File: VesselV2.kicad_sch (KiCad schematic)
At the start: 219 parts, among them SW1 SW_Push, U1 ATmega32U4-A, Y1 16MHz

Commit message: Switch footprint swap - 3d models fixed - Routing (re)done - No errors other than USB footprint
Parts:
- MX1, MX10, MX100, MX101, MX102, MX11, MX12, MX13, MX14, MX15, MX16, MX17, MX18, MX19, MX2, MX20, MX21, MX22, MX23, MX24, MX25, MX26, MX27, MX28, MX29, MX3, MX30, MX31, MX32, MX33, MX34, MX35, MX36, MX37, MX38, MX39, MX4, MX40, MX41, MX42, MX43, MX44, MX46, MX47, MX49, MX5, MX50, MX51, MX52, MX53, MX54, MX55, MX56, MX57, MX58, MX59, MX6, MX60, MX62, MX63, MX65, MX66, MX67, MX68, MX69, MX7, MX70, MX71, MX72, MX73, MX74, MX75, MX76, MX77, MX78, MX8, MX80, MX81, MX82, MX83, MX84, MX85, MX86, MX87, MX88, MX89, MX9, MX90, MX92, MX93: footprint PCM_marbastlib-mx:SW_MX_1u -> PCM_Switch_Keyboard_Cherry_MX:SW_Cherry_MX_PCB_1.00u
- MX45: footprint PCM_marbastlib-mx:SW_MX_1u -> PCM_Switch_Keyboard_Cherry_MX:SW_Cherry_MX_PCB_2.00u
- MX48: footprint PCM_marbastlib-mx:SW_MX_1.5u -> PCM_Switch_Keyboard_Cherry_MX:SW_Cherry_MX_PCB_1.50u
- MX61: footprint PCM_marbastlib-mx:SW_MX_1u -> PCM_Switch_Keyboard_Cherry_MX:SW_Cherry_MX_PCB_ISOEnter
- MX64, MX91: footprint PCM_marbastlib-mx:SW_MX_1.75u -> PCM_Switch_Keyboard_Cherry_MX:SW_Cherry_MX_PCB_1.75u
- MX79, MX94, MX95, MX96, MX98, MX99: footprint PCM_marbastlib-mx:SW_MX_1.25u -> PCM_Switch_Keyboard_Cherry_MX:SW_Cherry_MX_PCB_1.25u
- MX97: footprint PCM_marbastlib-mx:SW_MX_1u -> PCM_Switch_Keyboard_Cherry_MX:SW_Cherry_MX_PCB_6.25u
- S1: footprint PCM_marbastlib-mx:STAB_MX_P_2u -> PCM_Mounting_Keyboard_Stabilizer:Stabilizer_Cherry_MX_2.00u
- S2: footprint PCM_marbastlib-mx:STAB_MX_P_ISO -> PCM_Mounting_Keyboard_Stabilizer:Stabilizer_Cherry_MX_2.00u
- S3: footprint PCM_marbastlib-mx:STAB_MX_P_6.25u -> PCM_Mounting_Keyboard_Stabilizer:Stabilizer_Cherry_MX_6.25u

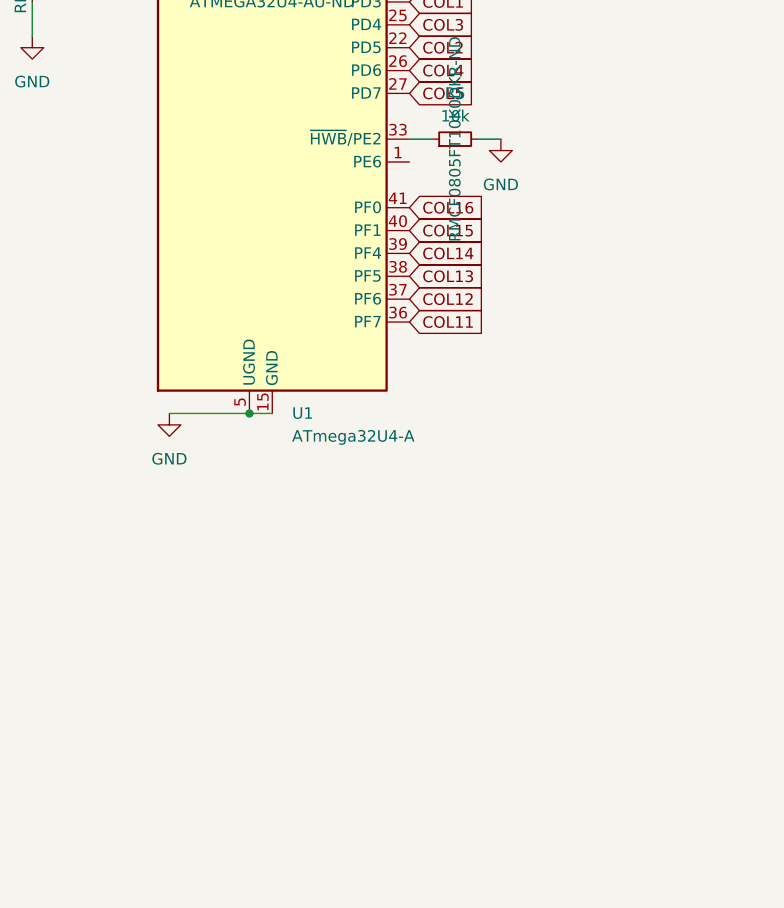
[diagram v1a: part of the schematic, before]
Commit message: Led Logo symbol and added - useless files deleted
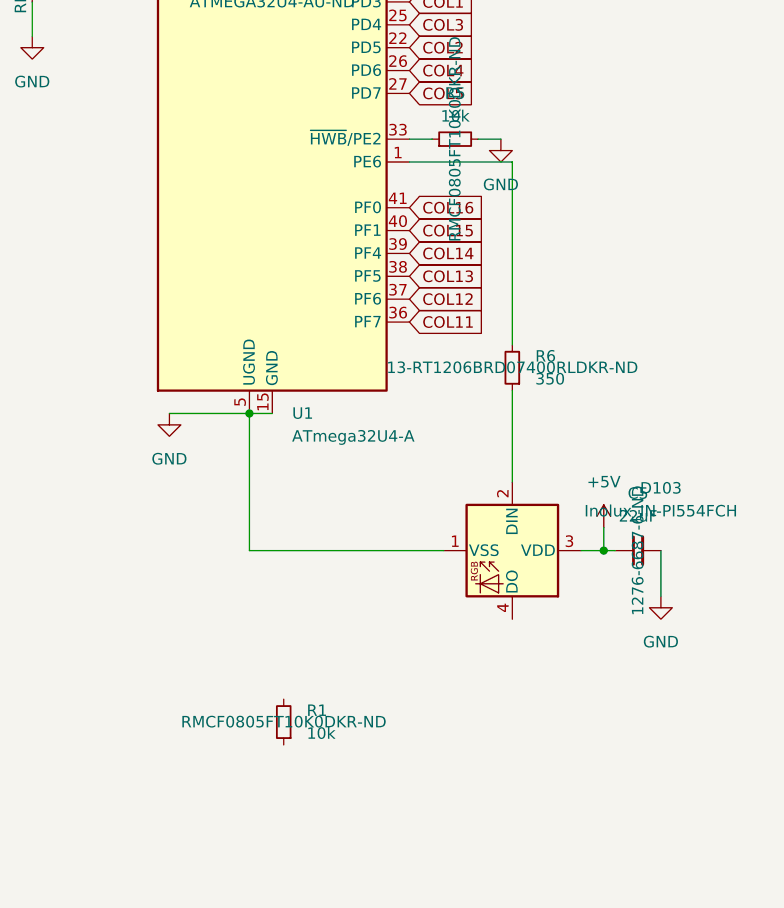
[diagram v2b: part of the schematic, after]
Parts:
- added C5: 22uF, Capacitor_SMD:C_0805_2012Metric_Pad1.18x1.45mm_HandSolder, symbol Device:C_Small
- added D103: Inolux_IN-PI554FCH, LED_SMD:LED_Inolux_IN-PI554FCH_PLCC4_5.0x5.0mm_P3.2mm, symbol LED:Inolux_IN-PI554FCH
- added R1: 10k, Resistor_SMD:R_0805_2012Metric_Pad1.20x1.40mm_HandSolder, symbol Device:R_Small
- added R6: 350, Resistor_SMD:R_0805_2012Metric_Pad1.20x1.40mm_HandSolder, symbol Device:R_Small
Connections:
- net +5V: now also C5.1, D103.3 (VDD)
- net GND: now also C5.2, D103.1 (VSS)
- net at U1.1 (PE6): now also R6.2
- new net: D103.2 (DIN), R6.1
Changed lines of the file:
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@@
   (junction (at 102.87 153.67) (diameter 0) (color 0 0 0 0)
   )
+  (junction (at 398.78 167.64) (diameter 0) (color 0 0 0 0)
+  )
   (junction (at 210.82 147.32) (diameter 0) (color 0 0 0 0)
   )
@@
     (stroke (width 0) (type default))
   )
+  (wire (pts (xy 388.62 149.86) (xy 388.62 160.02))
+    (stroke (width 0) (type default))
+  )
   (wire (pts (xy 176.53 198.12) (xy 187.96 198.12))
     (stroke (width 0) (type default))
@@
     (stroke (width 0) (type default))
   )
+  (wire (pts (xy 398.78 165.1) (xy 398.78 167.64))
+    (stroke (width 0) (type default))
+  )
   (wire (pts (xy 199.39 198.12) (xy 210.82 198.12))
     (stroke (width 0) (type default))
@@
     (stroke (width 0) (type default))
   )
+  (wire (pts (xy 405.13 167.64) (xy 405.13 172.72))
+    (stroke (width 0) (type default))
+  )
   (wire (pts (xy 210.82 147.32) (xy 222.25 147.32))
     (stroke (width 0) (type default))
@@
     (stroke (width 0) (type default))
   )
+  (wire (pts (xy 388.62 124.46) (xy 388.62 144.78))
+    (stroke (width 0) (type default))
+  )
   (wire (pts (xy 80.01 97.79) (xy 80.01 116.84))
     (stroke (width 0) (type default))
@@
     (stroke (width 0) (type default))
   )
+  (wire (pts (xy 398.78 167.64) (xy 400.05 167.64))
+    (stroke (width 0) (type default))
+  )
   (wire (pts (xy 182.88 137.16) (xy 182.88 153.67))
     (stroke (width 0) (type default))
@@
     (stroke (width 0) (type default))
   )
+  (wire (pts (xy 381 167.64) (xy 359.41 167.64))
+    (stroke (width 0) (type default))
+  )
   (wire (pts (xy 125.73 153.67) (xy 125.73 170.18))
     (stroke (width 0) (type default))
@@
     (stroke (width 0) (type default))
   )
+  (wire (pts (xy 396.24 167.64) (xy 398.78 167.64))
+    (stroke (width 0) (type default))
+  )
   (wire (pts (xy 303.53 35.56) (xy 309.88 35.56))
     (stroke (width 0) (type default))
@@
     (stroke (width 0) (type default))
   )
+  (wire (pts (xy 377.19 124.46) (xy 388.62 124.46))
+    (stroke (width 0) (type default))
+  )
   (wire (pts (xy 102.87 153.67) (xy 102.87 170.18))
     (stroke (width 0) (type default))
@@
     (stroke (width 0) (type default))
   )
+  (wire (pts (xy 359.41 167.64) (xy 359.41 152.4))
+    (stroke (width 0) (type default))
+  )
   (wire (pts (xy 129.54 116.84) (xy 129.54 137.16))
     (stroke (width 0) (type default))
@@
     )
   )
+  (symbol (lib_id "power:GND") (at 405.13 172.72 0) (unit 1)
+    (in_bom yes) (on_board yes) (dnp no) (fields_autoplaced)
+    (property "Reference" "#PWR013" (at 405.13 179.07 0)
+      (effects (font (size 1.27 1.27)) hide)
+    )
+    (property "Value" "GND" (at 405.13 177.8 0)
+      (effects (font (size 1.27 1.27)))
+    )
+    (property "Footprint" "" (at 405.13 172.72 0)
+      (effects (font (size 1.27 1.27)) hide)
+    )
+    (property "Datasheet" "" (at 405.13 172.72 0)
+      (effects (font (size 1.27 1.27)) hide)
+    )
+    (pin "1")
+    (instances
+      (project "VesselV2"
+        (path "/c445c6d8-4fde-4143-815a-ac483f9e4cc3"
+          (reference "#PWR013") (unit 1)
+        )
+      )
+    )
+  )
   (symbol (lib_id "Device:D_Small") (at 262.89 105.41 90) (unit 1)
     (in_bom yes) (on_board yes) (dnp no) (fields_autoplaced)
@@
     )
   )
+  (symbol (lib_id "Device:R_Small") (at 363.22 186.69 180) (unit 1)
+    (in_bom yes) (on_board yes) (dnp no) (fields_autoplaced)
+    (property "Reference" "R1" (at 365.76 185.42 0)
+      (effects (font (size 1.27 1.27)) (justify right))
+    )
+    (property "Value" "10k" (at 365.76 187.96 0)
+      (effects (font (size 1.27 1.27)) (justify right))
+    )
+    (property "Footprint" "Resistor_SMD:R_0805_2012Metric_Pad1.20x1.40mm_HandSolder" (at 363.22 186.69 0)
+      (effects (font (size 1.27 1.27)) hide)
+    )
+    (property "Datasheet" "~" (at 363.22 186.69 0)
+      (effects (font (size 1.27 1.27)) hide)
+    )
+    (property "DigikeyPartNumber" "RMCF0805FT10K0DKR-ND" (at 363.22 186.69 0)
+      (effects (font (size 1.27 1.27)))
+    )
+    (property "ManufacturerPartNumber" "" (at 363.22 186.69 0)
+      (effects (font (size 1.27 1.27)) hide)
+    )
+    (property "MouserPartNumber" "708-RMCF0805FT10K0" (at 363.22 186.69 0)
+      (effects (font (size 1.27 1.27)) hide)
+    )
+    (pin "1")
+    (pin "2")
+    (instances
+      (project "VesselV2"
+        (path "/c445c6d8-4fde-4143-815a-ac483f9e4cc3"
+          (reference "R1") (unit 1)
+        )
+      )
+    )
+  )
   (symbol (lib_id "Device:D_Small") (at 119.38 177.8 90) (unit 1)
     (in_bom yes) (on_board yes) (dnp no) (fields_autoplaced)
@@
     )
   )
+  (symbol (lib_id "power:+5V") (at 398.78 165.1 0) (unit 1)
+    (in_bom yes) (on_board yes) (dnp no) (fields_autoplaced)
+    (property "Reference" "#PWR012" (at 398.78 168.91 0)
+      (effects (font (size 1.27 1.27)) hide)
+    )
+    (property "Value" "+5V" (at 398.78 160.02 0)
+      (effects (font (size 1.27 1.27)))
+    )
+    (property "Footprint" "" (at 398.78 165.1 0)
+      (effects (font (size 1.27 1.27)) hide)
+    )
+    (property "Datasheet" "" (at 398.78 165.1 0)
+      (effects (font (size 1.27 1.27)) hide)
+    )
+    (pin "1")
+    (instances
+      (project "VesselV2"
+        (path "/c445c6d8-4fde-4143-815a-ac483f9e4cc3"
+          (reference "#PWR012") (unit 1)
+        )
+      )
+    )
+  )
   (symbol (lib_id "PCM_marbastlib-mx:MX_SW_solder") (at 151.13 207.01 0) (unit 1)
     (in_bom yes) (on_board yes) (dnp no) (fields_autoplaced)
@@
     )
   )
+  (symbol (lib_id "LED:Inolux_IN-PI554FCH") (at 388.62 167.64 270) (unit 1)
+    (in_bom yes) (on_board yes) (dnp no) (fields_autoplaced)
+    (property "Reference" "D103" (at 405.13 160.7119 90)
+      (effects (font (size 1.27 1.27)))
+    )
+    (property "Value" "Inolux_IN-PI554FCH" (at 405.13 163.2519 90)
+      (effects (font (size 1.27 1.27)))
+    )
+    (property "Footprint" "LED_SMD:LED_Inolux_IN-PI554FCH_PLCC4_5.0x5.0mm_P3.2mm" (at 381 168.91 0)
+      (effects (font (size 1.27 1.27)) (justify left top) hide)
+    )
+    (property "Datasheet" "http://www.inolux-corp.com/datasheet/SMDLED/Addressable%20LED/IN-PI554FCH.pdf" (at 379.095 170.18 0)
+      (effects (font (size 1.27 1.27)) (justify left top) hide)
+    )
+    (pin "1")
+    (pin "2")
+    (pin "3")
+    (pin "4")
+    (instances
+      (project "VesselV2"
+        (path "/c445c6d8-4fde-4143-815a-ac483f9e4cc3"
+          (reference "D103") (unit 1)
+        )
+      )
+    )
+  )
   (symbol (lib_id "Device:D_Small") (at 274.32 124.46 90) (unit 1)
     (in_bom yes) (on_board yes) (dnp no) (fields_autoplaced)
@@
     )
   )
+  (symbol (lib_id "Device:C_Small") (at 402.59 167.64 90) (unit 1)
+    (in_bom yes) (on_board yes) (dnp no) (fields_autoplaced)
+    (property "Reference" "C5" (at 402.5963 161.29 90)
+      (effects (font (size 1.27 1.27)))
+    )
+    (property "Value" "22uF" (at 402.5963 163.83 90)
+      (effects (font (size 1.27 1.27)))
+    )
+    (property "Footprint" "Capacitor_SMD:C_0805_2012Metric_Pad1.18x1.45mm_HandSolder" (at 402.59 167.64 0)
+      (effects (font (size 1.27 1.27)) hide)
+    )
+    (property "Datasheet" "https://www.samsungsem.com/kr/support/product-search/mlcc/CL21A226KQCLRNC.jsp" (at 402.59 167.64 0)
+      (effects (font (size 1.27 1.27)) hide)
+    )
+    (property "DigikeyPartNumber" "1276-6687-6-ND" (at 402.59 167.64 0)
+      (effects (font (size 1.27 1.27)))
+    )
+    (property "ManufacturerPartNumber" "" (at 402.59 167.64 0)
+      (effects (font (size 1.27 1.27)) hide)
+    )
+    (property "MouserPartNumber" "187-CL21A226KQCLRNC" (at 402.59 167.64 0)
+      (effects (font (size 1.27 1.27)) hide)
+    )
+    (pin "1")
+    (pin "2")
+    (instances
+      (project "VesselV2"
+        (path "/c445c6d8-4fde-4143-815a-ac483f9e4cc3"
+          (reference "C5") (unit 1)
+        )
+      )
+    )
+  )
   (symbol (lib_id "PCM_marbastlib-mx:MX_SW_solder") (at 82.55 190.5 0) (unit 1)
     (in_bom yes) (on_board yes) (dnp no) (fields_autoplaced)
@@
         )
       )
+    )
+  )
+  (symbol (lib_id "Device:R_Small") (at 388.62 147.32 180) (unit 1)
+    (in_bom yes) (on_board yes) (dnp no) (fields_autoplaced)
+    (property "Reference" "R6" (at 391.16 146.05 0)
+      (effects (font (size 1.27 1.27)) (justify right))
+    )
+    (property "Value" "350" (at 391.16 148.59 0)
+      (effects (font (size 1.27 1.27)) (justify right))
+    )
+    (property "Footprint" "Resistor_SMD:R_0805_2012Metric_Pad1.20x1.40mm_HandSolder" (at 388.62 147.32 0)
+      (effects (font (size 1.27 1.27)) hide)
+    )
+    (property "Datasheet" "https://www.mouser.com/datasheet/2/447/PYu_RT_1_to_0_01_RoHS_L_12-3003070.pdf" (at 388.62 147.32 0)
+      (effects (font (size 1.27 1.27)) hide)
+    )
+    (property "DigikeyPartNumber" "13-RT1206BRD07400RLDKR-ND" (at 388.62 147.32 0)
+      (effects (font (size 1.27 1.27)))
+    )
+    (property "ManufacturerPartNumber" "RT1206BRD07400RL" (at 388.62 147.32 0)
+      (effects (font (size 1.27 1.27)) hide)
+    )
+    (property "MouserPartNumber" "603-RT1206BRD07400RL " (at 388.62 147.32 0)
+      (effects (font (size 1.27 1.27)) hide)
+    )
+    (pin "1")
+    (pin "2")
+    (instances
+      (project "VesselV2"
+        (path "/c445c6d8-4fde-4143-815a-ac483f9e4cc3"
+          (reference "R6") (unit 1)
+        )
+      )

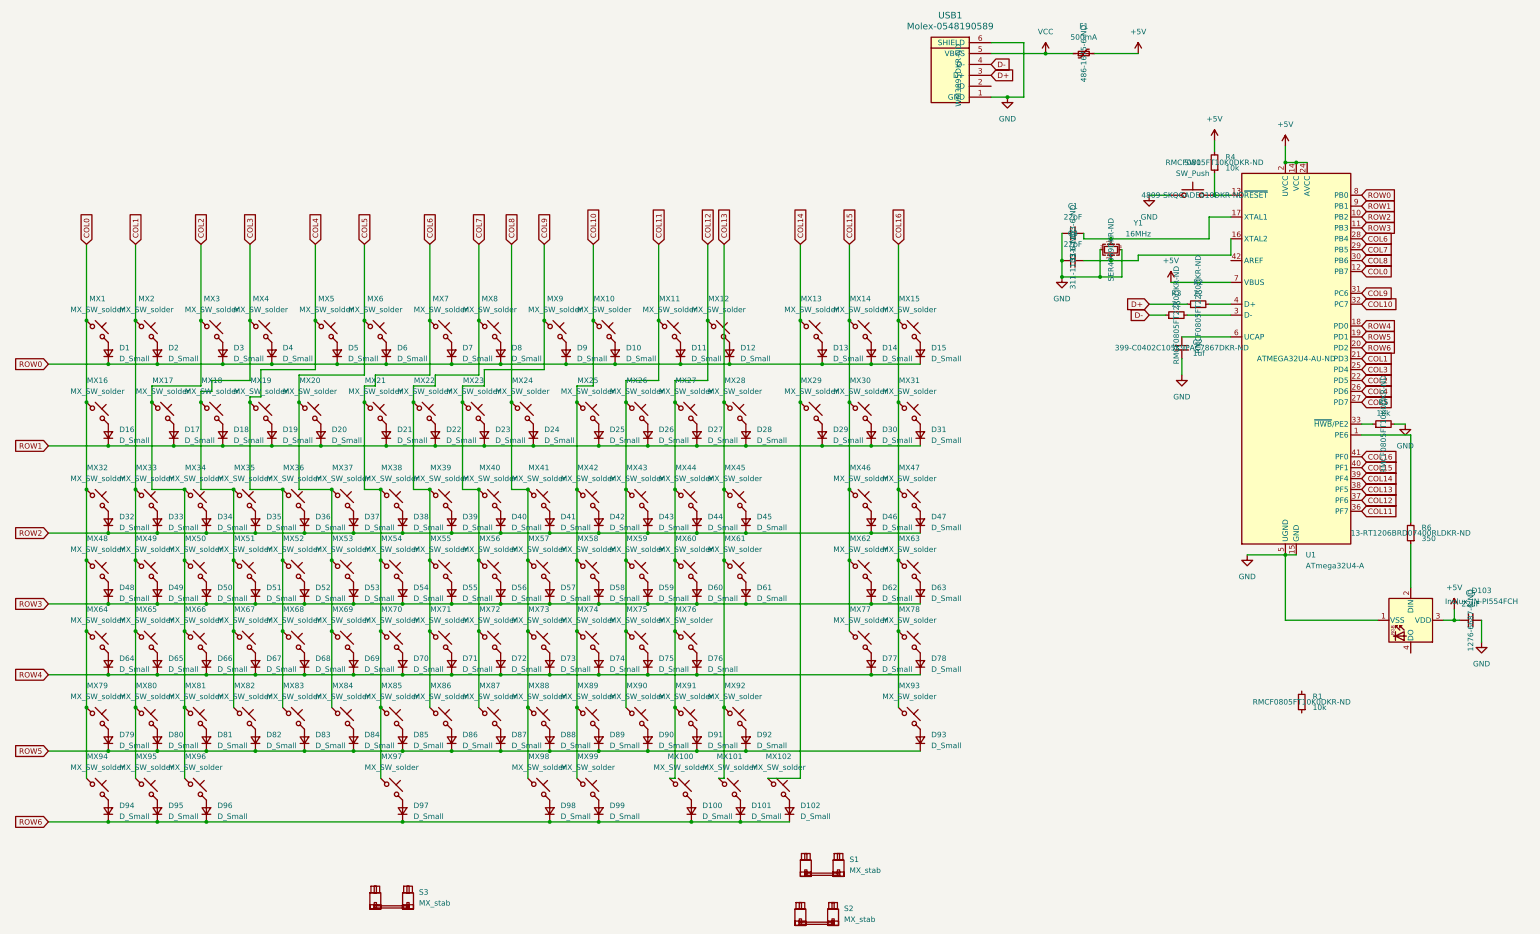
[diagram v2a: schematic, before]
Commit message: USB connector swap and rerouting - No more errors
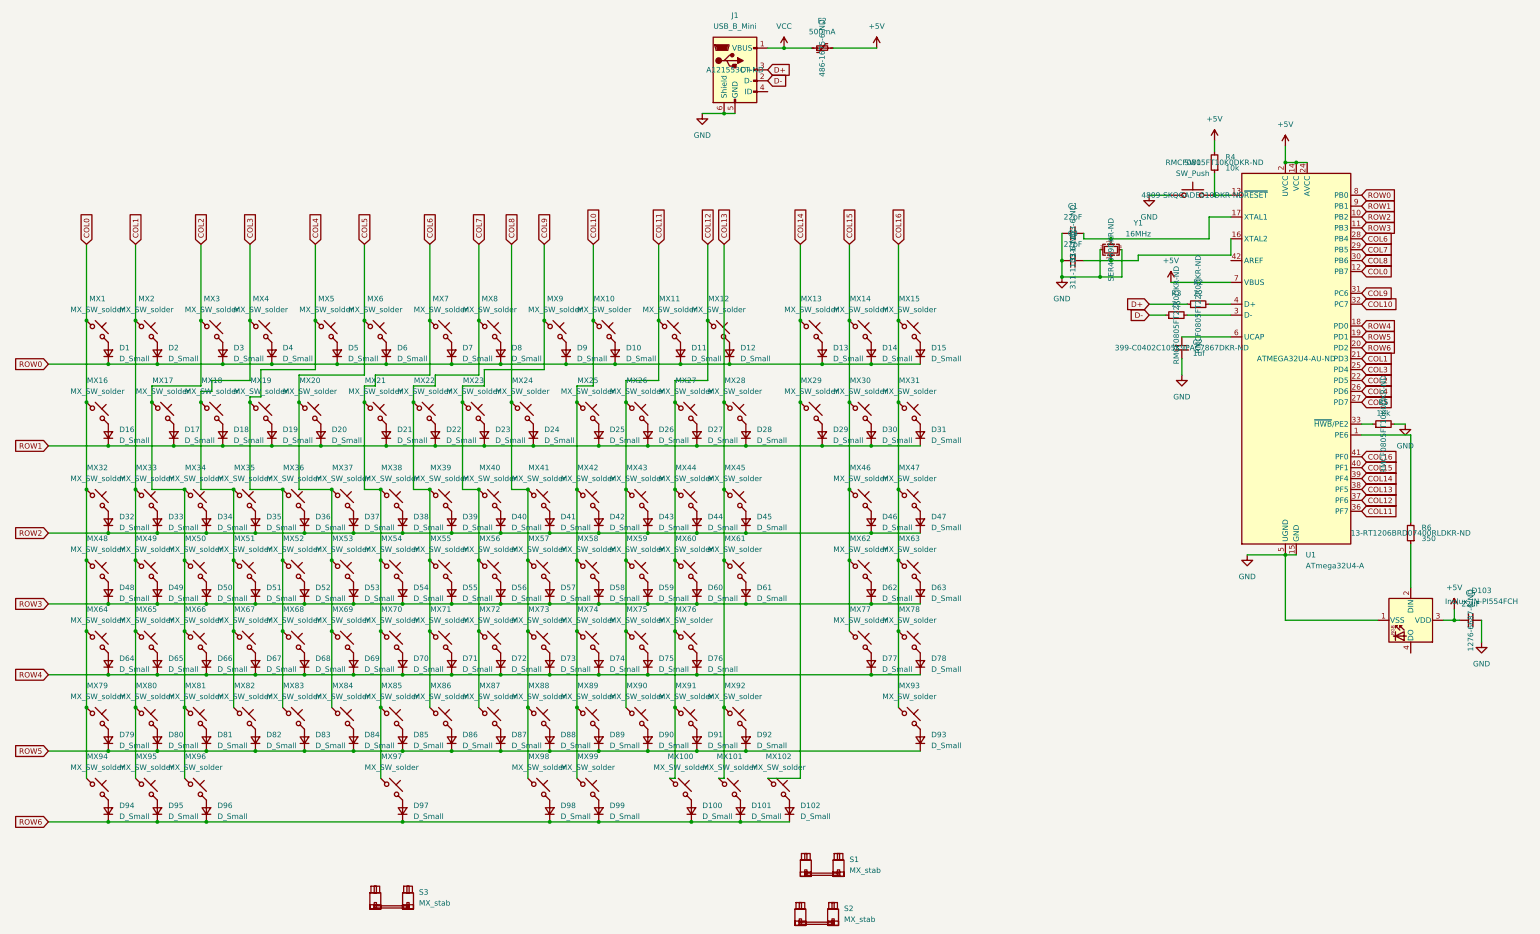
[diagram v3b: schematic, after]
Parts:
- removed F1: 500mA, Fuse:Fuse_1206_3216Metric_Pad1.42x1.75mm_HandSolder, symbol Device:Polyfuse_Small
- removed R1: 10k, Resistor_SMD:R_0805_2012Metric_Pad1.20x1.40mm_HandSolder, symbol Device:R_Small
- removed USB1: Molex-0548190589, random-keyboard-parts:Molex-0548190589, symbol random-keyboard-parts:Molex-0548190589
- added F2: 500mA, Fuse:Fuse_1206_3216Metric_Pad1.42x1.75mm_HandSolder, symbol Device:Polyfuse_Small
- added J1: USB_B_Mini, Connector_USB:USB_Mini-B_Lumberg_2486_01_Horizontal, symbol Connector:USB_B_Mini
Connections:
- net +5V: now also F2.2
- net D+: now also J1.3 (D+)
- net D-: now also J1.2 (D-)
- net GND: now also J1.5 (GND), J1.6 (Shield)
- net VCC: now also F2.1, J1.1 (VBUS)
